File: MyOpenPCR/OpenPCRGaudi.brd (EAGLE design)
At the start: 61.9 x 83.2 mm, 14 parts, among them IC1 MCP3551SN, IC2 VNH3SP30_2, Q2 BSS97

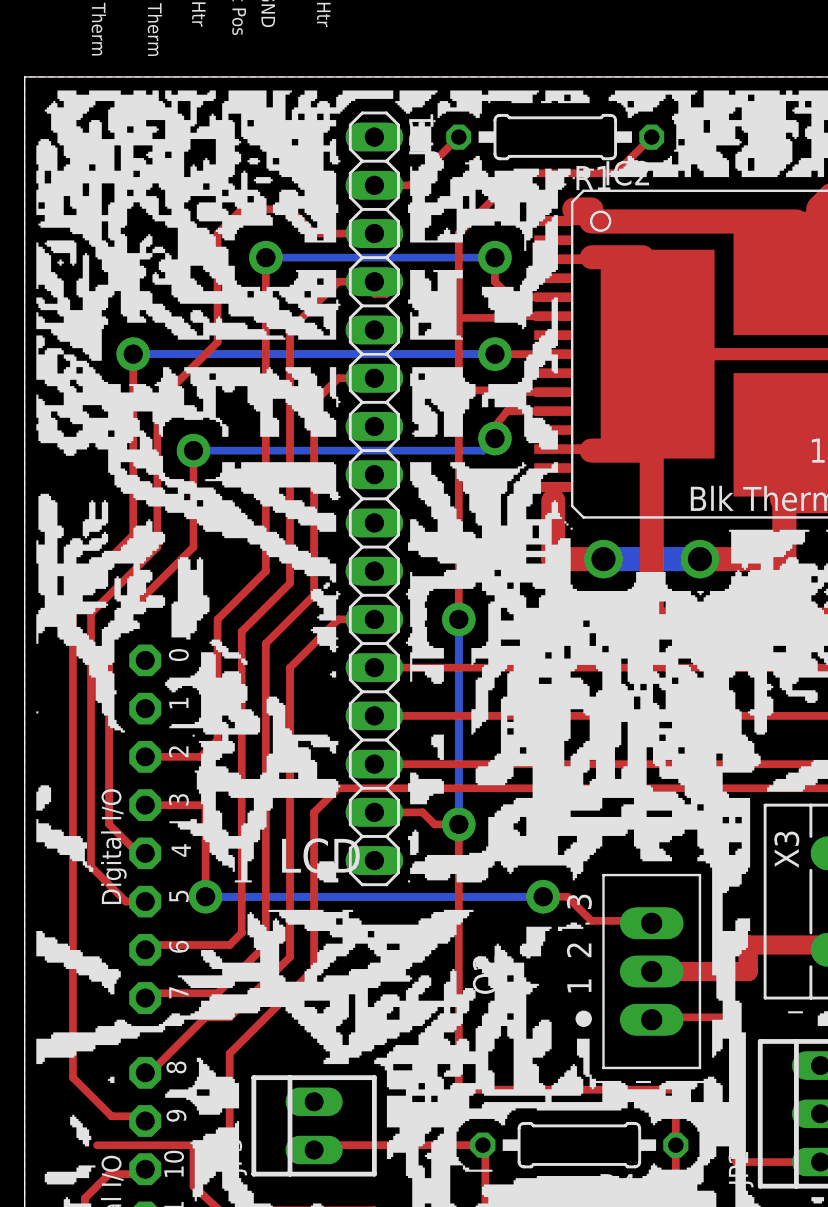
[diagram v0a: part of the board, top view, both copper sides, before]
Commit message: fixed an error on the PCB and added new Code
for two line LCD and different temp sensor.
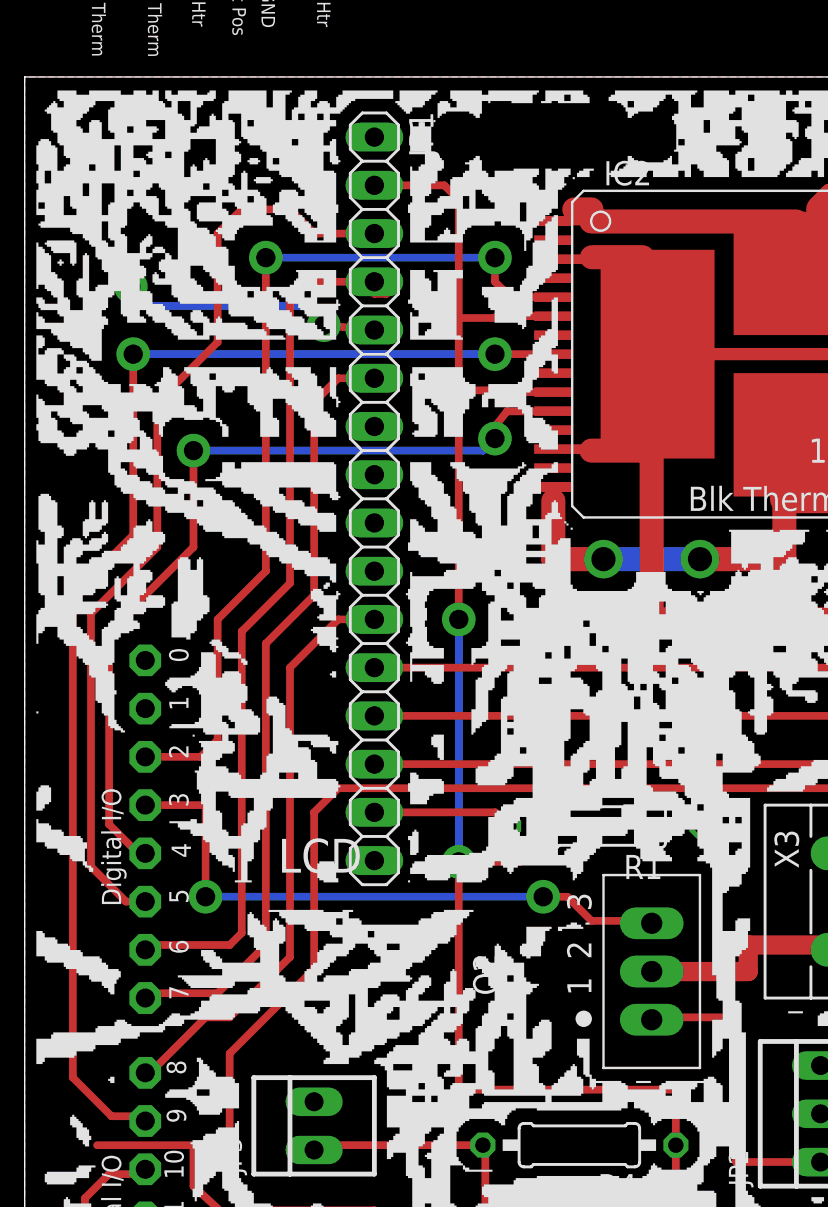
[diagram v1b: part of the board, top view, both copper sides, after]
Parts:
- moved R1 36.4 mm to (30.6, 43.7)
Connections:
- removed net N$1: JP1.2, R1.2
- new net N$5: JP1.15, R1.2
- net +5VREG: now also JP1.2; no longer JP1.15
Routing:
- net GND1: track 51.8 -> 66.6 mm, vias 0 -> 2
- net N$5: track 0.00 -> 7.37 mm
- net N$1: track 5.50 -> 0.00 mm
- net +5VREG: track 172.2 -> 175.4 mm
- net N$3: track 46.3 -> 47.2 mm
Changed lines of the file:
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@@
 <setting verticaltext="up"/>
 </settings>
-<grid distance="0.109601" unitdist="mm" unit="mm" style="lines" multiple="1" display="yes" altdistance="0.025" altunitdist="inch" altunit="inch"/>
+<grid distance="20" unitdist="mil" unit="mil" style="lines" multiple="1" display="yes" altdistance="0.025" altunitdist="inch" altunit="inch"/>
 <layers>
 <layer number="1" name="Top" color="4" fill="1" visible="yes" active="yes"/>
@@
 <layer number="19" name="Unrouted" color="13" fill="1" visible="yes" active="yes"/>
 <layer number="20" name="Dimension" color="15" fill="1" visible="yes" active="yes"/>
-<layer number="21" name="tPlace" color="7" fill="1" visible="yes" active="yes"/>
+<layer number="21" name="tPlace" color="7" fill="1" visible="no" active="yes"/>
 <layer number="22" name="bPlace" color="7" fill="1" visible="no" active="yes"/>
 <layer number="23" name="tOrigins" color="15" fill="1" visible="yes" active="yes"/>
@@
 <attribute name="OC_NEWARK" value="unknown" x="43.815" y="39.751" size="1.778" layer="27" rot="R270" display="off"/>
 </element>
-<element name="R1" library="resistor" package="0207/10" value="" x="27.94" y="80.01" rot="R180"/>
+<element name="R1" library="resistor" package="0207/10" value="" x="30.570425" y="43.73206875" rot="R180"/>
 </elements>
 <signals>
@@
 <vertex x="0" y="83.185"/>
 </polygon>
+<wire x1="18.415" y1="69.85" x2="15.748" y2="70.104" width="0.4064" layer="1"/>
+<via x="15.748" y="70.104" extent="1-16" drill="1.016" diameter="1.778" shape="square"/>
+<wire x1="15.748" y1="70.104" x2="14.732" y2="71.12" width="0.4064" layer="16"/>
+<wire x1="14.732" y1="71.12" x2="5.588" y2="71.12" width="0.4064" layer="16"/>
+<wire x1="5.588" y1="71.12" x2="5.588" y2="72.136" width="0.4064" layer="16"/>
+<via x="5.588" y="72.136" extent="1-16" drill="1.016" diameter="1.778" shape="square"/>
+<wire x1="5.588" y1="72.136" x2="5.588" y2="71.628" width="0.4064" layer="1"/>
 </signal>
 <signal name="+12V1" class="2">
@@
 </signal>
 <signal name="+5VREG" class="1">
-<contactref element="JP1" pad="15"/>
 <contactref element="R4" pad="1"/>
 <contactref element="R10" pad="2"/>
@@
 <wire x1="34.29" y1="19.05" x2="34.29" y2="26.924" width="0.4064" layer="1"/>
 <wire x1="25.019" y1="66.58" x2="27.83" y2="66.58" width="0.4064" layer="1"/>
-<wire x1="22.86" y1="43.815" x2="22.86" y2="54.61" width="0.4064" layer="16"/>
+<wire x1="22.86" y1="41.84218125" x2="22.86" y2="54.61" width="0.4064" layer="16"/>
 <wire x1="34.29" y1="26.924" x2="34.29" y2="29.845" width="0.4064" layer="1"/>
 <wire x1="34.29" y1="29.845" x2="22.86" y2="29.845" width="0.4064" layer="1"/>
-<wire x1="22.86" y1="29.845" x2="22.86" y2="43.815" width="0.4064" layer="1"/>
+<wire x1="22.86" y1="29.845" x2="22.86" y2="41.84218125" width="0.4064" layer="1"/>
 <wire x1="17.653" y1="8.322" x2="17.653" y2="13.522" width="0.4064" layer="1"/>
 <wire x1="17.653" y1="8.322" x2="17.78" y2="8.322" width="0.4064" layer="1"/>
@@
 <wire x1="57.785" y1="27.051" x2="57.658" y2="27.178" width="0.4064" layer="1"/>
 <wire x1="22.86" y1="66.675" x2="22.86" y2="70.485" width="0.4064" layer="1"/>
-<wire x1="22.86" y1="70.485" x2="22.86" y2="74.93" width="0.4064" layer="1"/>
-<wire x1="22.86" y1="74.93" x2="26.035" y2="78.105" width="0.4064" layer="1"/>
-<wire x1="26.035" y1="78.105" x2="31.115" y2="78.105" width="0.4064" layer="1"/>
-<wire x1="31.115" y1="78.105" x2="33.02" y2="80.01" width="0.4064" layer="1"/>
-<wire x1="22.86" y1="43.815" x2="21.59" y2="43.815" width="0.4064" layer="1"/>
-<wire x1="21.59" y1="43.815" x2="20.955" y2="44.45" width="0.4064" layer="1"/>
-<wire x1="20.955" y1="44.45" x2="18.415" y2="44.45" width="0.4064" layer="1"/>
 <wire x1="22.86" y1="70.485" x2="24.765" y2="70.485" width="0.4064" layer="1"/>
 <wire x1="24.765" y1="70.485" x2="24.86" y2="70.58" width="0.4064" layer="1"/>
 <via x="22.86" y="54.61" extent="1-16" drill="1.016" diameter="1.778" shape="square"/>
-<via x="22.86" y="43.815" extent="1-16" drill="1.016" diameter="1.778" shape="square"/>
+<via x="22.86" y="41.84218125" extent="1-16" drill="1.016" diameter="1.778" shape="square"/>
+<contactref element="JP1" pad="2"/>
+<wire x1="22.86" y1="41.84218125" x2="26.0596375" y2="41.84218125" width="0.4064" layer="1"/>
+<wire x1="26.0596375" y1="41.84218125" x2="28.05785625" y2="43.8404" width="0.4064" layer="1"/>
+<wire x1="28.05785625" y1="43.8404" x2="35.54209375" y2="43.8404" width="0.4064" layer="1"/>
+<wire x1="35.54209375" y1="43.8404" x2="35.650425" y2="43.73206875" width="0.4064" layer="1"/>
+<wire x1="18.415" y1="77.47" x2="22.098" y2="77.47" width="0.4064" layer="1"/>
+<wire x1="22.098" y1="77.47" x2="22.86" y2="76.708" width="0.4064" layer="1"/>
+<wire x1="22.86" y1="76.708" x2="22.86" y2="70.485" width="0.4064" layer="1"/>
 </signal>
 <signal name="N$11">
@@
 <contactref element="JP1" pad="4"/>
 <contactref element="U$3" pad="D6"/>
-<wire x1="16.51" y1="72.39" x2="18.415" y2="72.39" width="0.4064" layer="1"/>
+<wire x1="14.986" y1="72.39" x2="18.415" y2="72.39" width="0.4064" layer="1"/>
 <wire x1="18.415" y1="72.39" x2="19.05" y2="72.39" width="0.4064" layer="1"/>
 <wire x1="19.05" y1="72.39" x2="19.05" y2="71.755" width="0.4064" layer="1"/>
@@
 <wire x1="11.43" y1="38.1" x2="11.43" y2="53.975" width="0.4064" layer="1"/>
 <wire x1="11.43" y1="53.975" x2="13.97" y2="56.515" width="0.4064" layer="1"/>
-<wire x1="13.97" y1="56.515" x2="13.97" y2="69.85" width="0.4064" layer="1"/>
-<wire x1="13.97" y1="69.85" x2="16.51" y2="72.39" width="0.4064" layer="1"/>
+<wire x1="13.97" y1="56.515" x2="13.97" y2="71.374" width="0.4064" layer="1"/>
+<wire x1="14.986" y1="72.39" x2="13.97" y2="71.374" width="0.4064" layer="1"/>
 </signal>
 <signal name="N$4">
@@
 <wire x1="43.18" y1="37.465" x2="43.18" y2="37.211" width="1.016" layer="1"/>
 </signal>
-<signal name="N$1" class="1">
+<signal name="N$5">
 <contactref element="R1" pad="2"/>
-<contactref element="JP1" pad="2"/>
-<wire x1="18.415" y1="77.47" x2="20.32" y2="77.47" width="0.4064" layer="1"/>
-<wire x1="20.32" y1="77.47" x2="22.86" y2="80.01" width="0.4064" layer="1"/>
+<contactref element="JP1" pad="15"/>
+<wire x1="18.415" y1="44.45" x2="24.77249375" y2="44.45" width="0.4064" layer="1"/>
+<wire x1="24.77249375" y1="44.45" x2="25.490425" y2="43.73206875" width="0.4064" layer="1"/>
 </signal>
 </signals>
